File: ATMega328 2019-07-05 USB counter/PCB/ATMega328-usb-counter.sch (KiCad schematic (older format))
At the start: 38 parts, among them J1 Conn_01x05_Male, J2 USB MINI, J3 Conn_01x02_Male, J4 RF, J5 Conn_01x02_Male, J6 Conn_01x02_Male, U1 FT230XS, U2 ATmega328PB-AU, U3 74LV8154, Y1 10 MHz

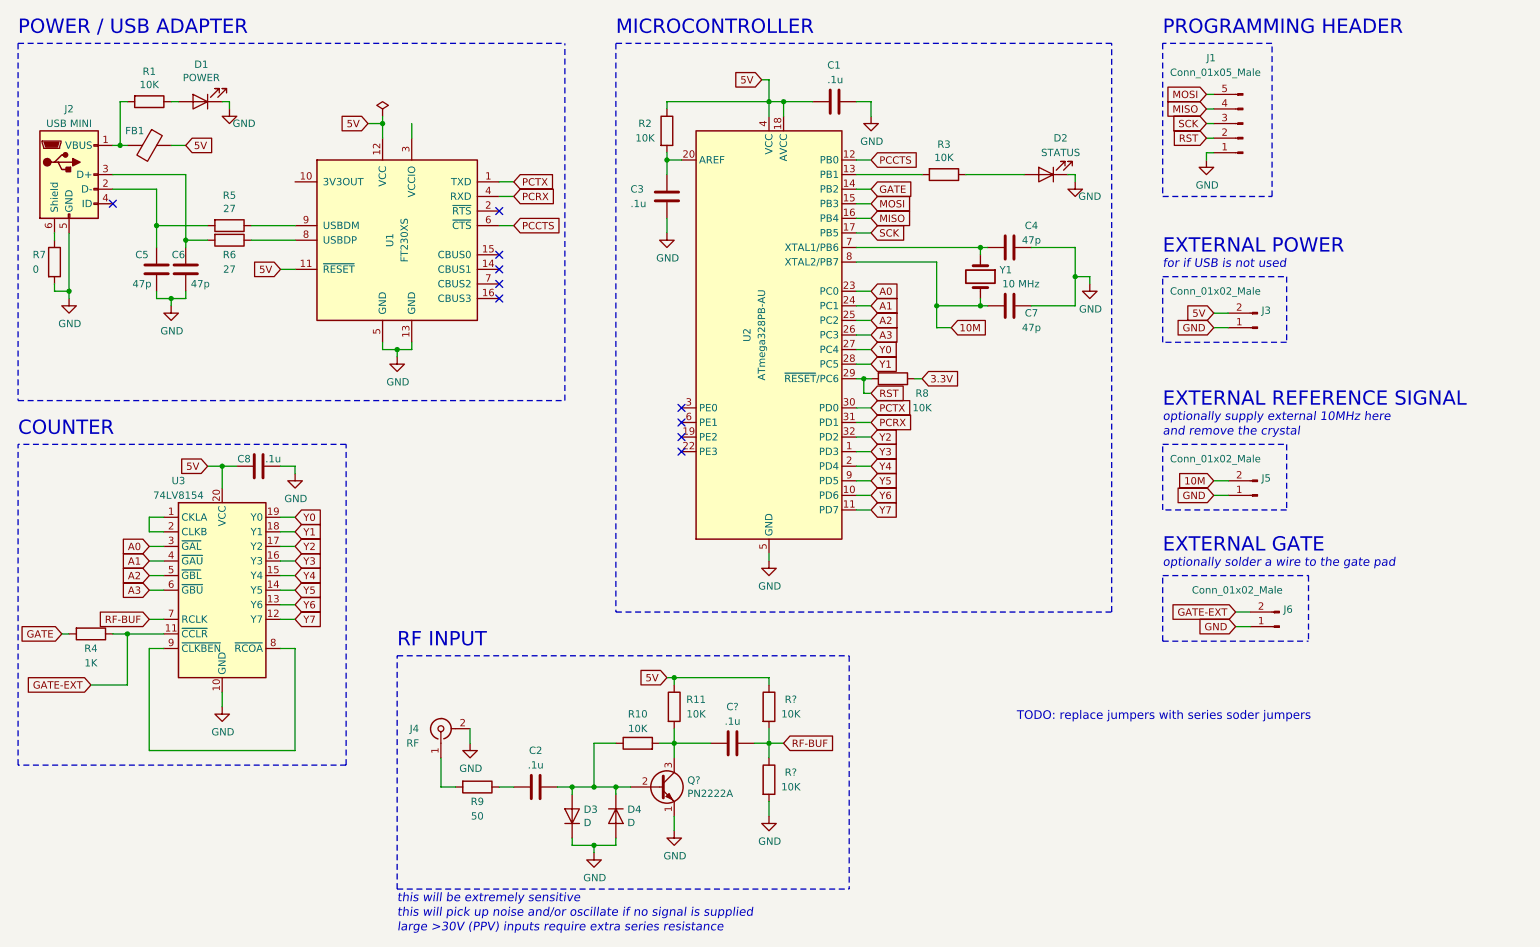
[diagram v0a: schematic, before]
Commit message: USB counter PCB
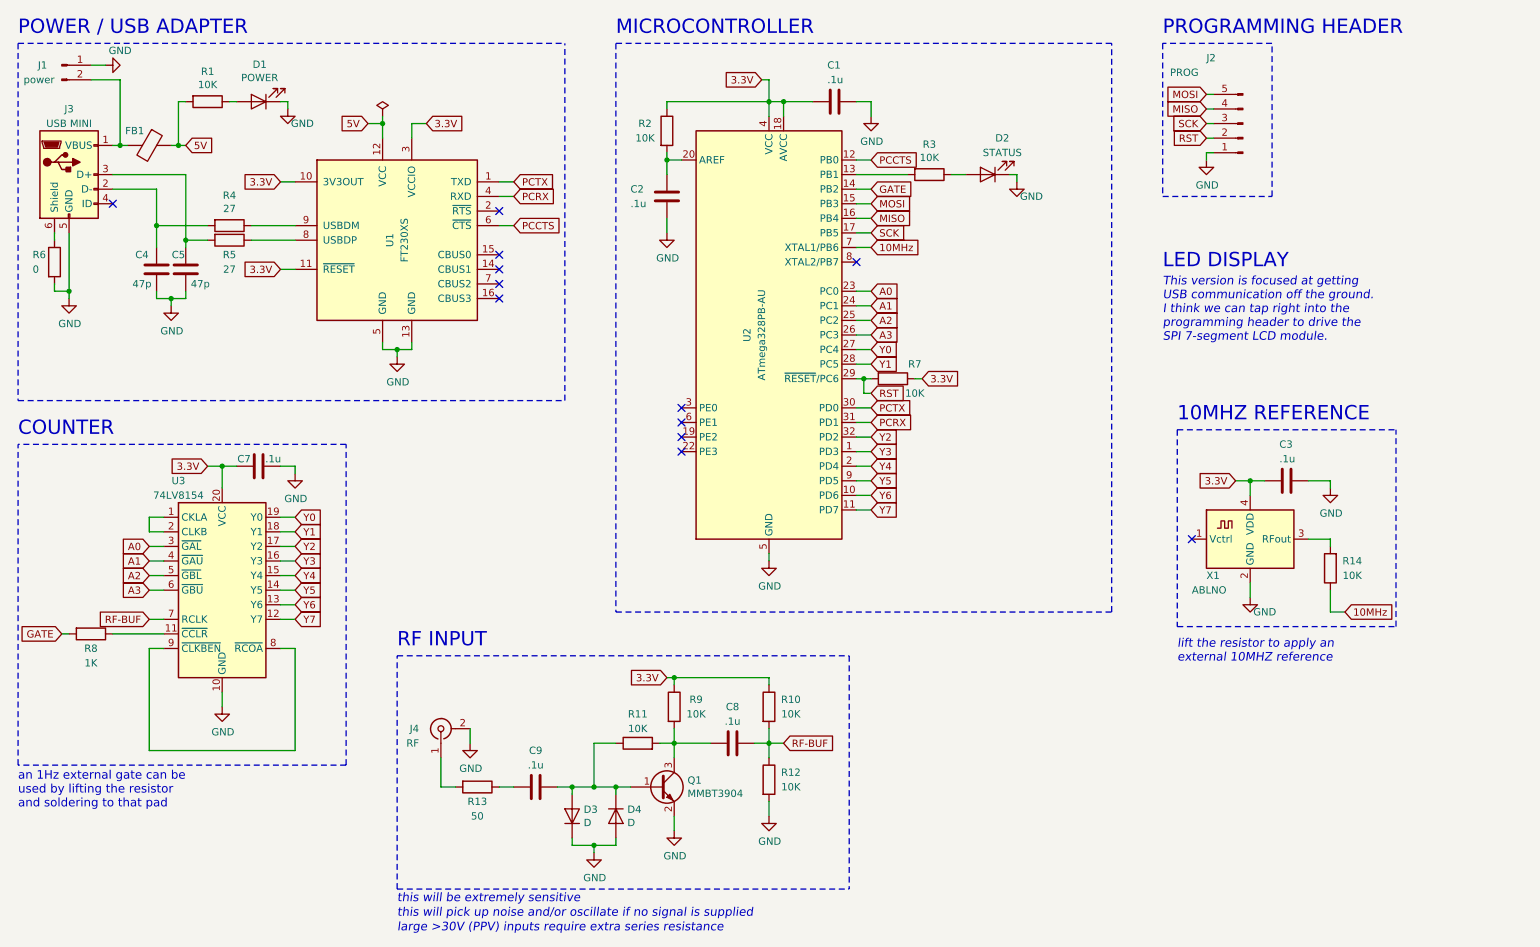
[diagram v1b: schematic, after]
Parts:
- removed C4, C7: 47p, Capacitor_SMD:C_0805_2012Metric_Pad1.15x1.40mm_HandSolder, symbol Device:C
- removed J5, J6: Conn_01x02_Male, symbol Connector:Conn_01x02_Male
- removed Q?: PN2222A, Package_TO_SOT_THT:TO-92_Inline, symbol Transistor_BJT:PN2222A
- removed Y1: 10 MHz, Crystal:Crystal_SMD_HC49-SD, symbol Device:Crystal
- added C3: .1u, Capacitor_SMD:C_0805_2012Metric_Pad1.15x1.40mm_HandSolder, symbol Device:C
- added Q1: MMBT3904, Package_TO_SOT_SMD:SOT-23, symbol Transistor_BJT:MMBT3904
- added R14: 10K, Resistor_SMD:R_0805_2012Metric_Pad1.15x1.40mm_HandSolder, symbol Device:R
- added X1: ABLNO, Oscillator:Oscillator_SMD_TXC_7C-4Pin_5.0x3.2mm_HandSoldering, symbol Oscillator:ABLNO
- D3, D4: footprint (none) -> Diode_SMD:D_0805_2012Metric_Pad1.15x1.40mm_HandSolder
- J1: renamed from J3; value Conn_01x02_Male -> power; footprint (none) -> Connector_PinHeader_2.54mm:PinHeader_1x02_P2.54mm_Vertical
- J2: renamed from J1; value Conn_01x05_Male -> PROG
- J4: footprint (none) -> Connector_Coaxial:SMA_Amphenol_901-144_Vertical
- U3: footprint (none) -> Package_SO:TSSOP-20_4.4x6.5mm_P0.65mm
- gave numbers to parts that had none: 3
- renumbered C3 to C2, C5 to C4, C6 to C5, C8 to C7, C2 to C9, J2 to J3, R10 to R11, R9 to R13, R5 to R4, R6 to R5, R7 to R6, R8 to R7, R4 to R8, R11 to R9
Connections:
- net 3.3V: now also C1.1, C7.1, R10.1, R2.1, R9.1, U1.10 (3V3OUT), U1.11 (~RESET), U1.3 (VCCIO), U2.18 (AVCC), U2.4 (VCC), U3.20 (VCC), C3.1, X1.4 (VDD)
- net 5V: now also R1.2; no longer C1.1, C7.1, J1.2 (Pin_2), R10.1, R2.1, R9.1, U1.11 (~RESET), U2.18 (AVCC), U2.4 (VCC), U3.20 (VCC)
- net GND: now also C3.2, Q1.2 (E), X1.2 (GND)
- net at FB1.2, J3.1 (VBUS): now also J1.2 (Pin_2); no longer R1.2
- net 10MHz: now reaches U2.7 (XTAL1/PB6)
- net 10MHz: now also R14.1
- net at C9.1, D3.2 (A), D4.1 (K)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: now also Q1.1 (B)
- net at C8.2, R11.2, R9.2: now also Q1.3 (C)
- net 10M: no longer names the net of U2.8 (XTAL2/PB7)
- net GATE-EXT: no longer names the net of R8.1, U3.11 (~CCLR)
- new net: R14.2, X1.3 (RFout)
- no-connect marks 10 -> 12
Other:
- note added: "10MHZ REFERENCE"
- note added: "LED DISPLAY"
- note added: "This version is focused at getting\nUSB communication off the ground.\nI think we can tap right into the\nprogramming header to drive the\nSPI 7-segment LCD module."
- note added: "an 1Hz external gate can be\nused by lifting the resistor\nand soldering to that pad"
- note added: "lift the resistor to apply an\nexternal 10MHZ reference"
- note removed: "EXTERNAL GATE"
- note removed: "EXTERNAL POWER"
- note removed: "EXTERNAL REFERENCE SIGNAL"
- note removed: "TODO: replace jumpers with series soder jumpers"
- note removed: "and remove the crystal"
- note removed: "for if USB is not used"
- note removed: "optionally solder a wire to the gate pad"
- note removed: "optionally supply external 10MHz here"
- moved on the sheet: D1, D2, J1, R1, R3

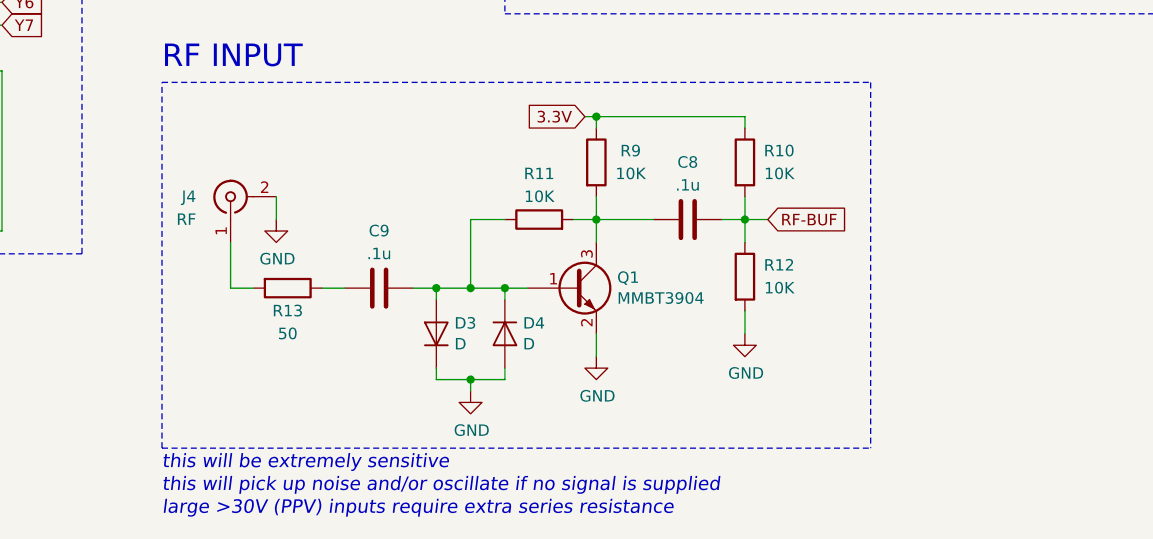
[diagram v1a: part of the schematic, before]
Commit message: improve PCB
higher impedance front-end, improved silkscreen
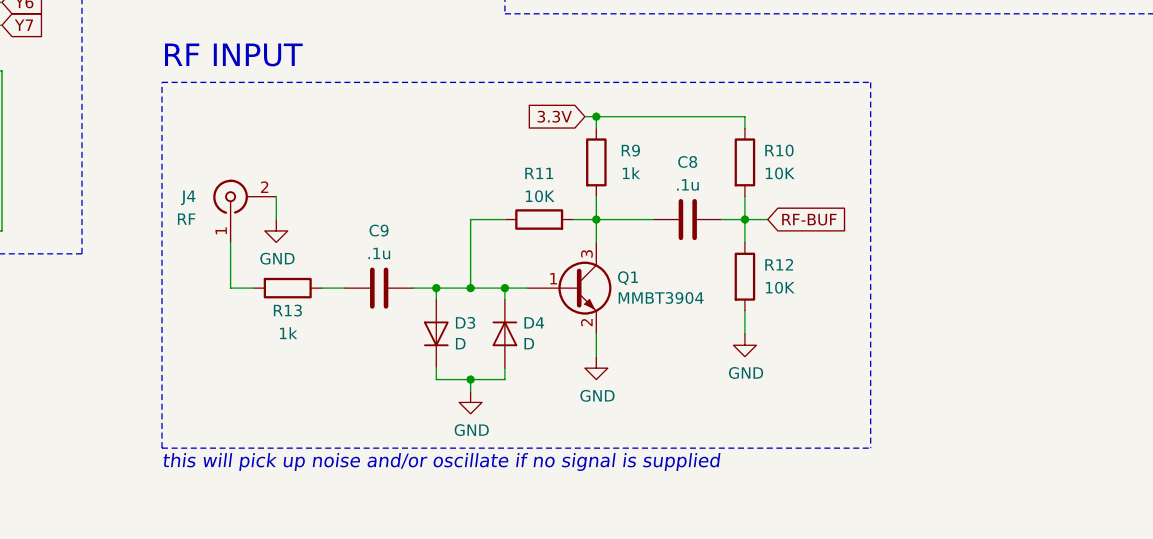
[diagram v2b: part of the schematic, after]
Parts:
- R13: value 50 -> 1k
- R9: value 10K -> 1k
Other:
- note removed: "large >30V (PPV) inputs require extra series resistance"
- note removed: "this will be extremely sensitive"
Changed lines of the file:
@@
 P 4050 6000
 F 0 "R13" V 4150 6000 50  0000 C CNN
-F 1 "50" V 4250 6000 50  0000 C CNN
+F 1 "1k" V 4250 6000 50  0000 C CNN
 F 2 "Resistor_SMD:R_0805_2012Metric_Pad1.15x1.40mm_HandSolder" V 3980 6000 50  0001 C CNN
 F 3 "~" H 4050 6000 50  0001 C CNN
@@
 P 5400 5450
 F 0 "R9" H 5550 5500 50  0000 C CNN
-F 1 "10K" H 5550 5400 50  0000 C CNN
+F 1 "1k" H 5550 5400 50  0000 C CNN
 F 2 "Resistor_SMD:R_0805_2012Metric_Pad1.15x1.40mm_HandSolder" V 5330 5450 50  0001 C CNN
 F 3 "~" H 5400 5450 50  0001 C CNN
@@
 	5400 5300 5400 5250
 Text Notes 3500 6800 0    59   Italic 0
-this will be extremely sensitive
-Text Notes 3500 6900 0    59   Italic 0
 this will pick up noise and/or oscillate if no signal is supplied
 $Comp
@@
 Wire Notes Line
 	3500 6700 6600 6700
-Text Notes 3500 7000 0    59   Italic 0
-large >30V (PPV) inputs require extra series resistance
 Wire Wire Line
 	1550 4950 1900 4950
